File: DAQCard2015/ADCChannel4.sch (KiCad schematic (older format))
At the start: 50 parts, among them U1 LTC6403, U2 AD9219, U3 LTC6403, U4 LTC6403, U5 LTC6403

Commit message: Updates to DAQ Card including FPGA card pinout and completion of ADC Stage
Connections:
- net labels added: 18ana

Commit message: Replaces single ample with 4-channel varients. Greatly reducing part count
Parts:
- removed C1, C11, C15, C16: .01uF, symbol C
- removed C10, C2, C3, C7, C9: .1uF, symbol C
- removed C12, C13, C14, C17, C18, C19, C20, C21, C4, C5, C6: C, symbol C
- removed C8: 2.2uF, symbol CP
- removed R1, R13, R14, R8: Rt, symbol R
- removed R10, R15, R16, R17, R2, R3, R9: Ri, symbol R
- removed R11, R12, R5, R6: Rf, symbol R
- removed R7: 10k, symbol R
- removed U1, U3, U4, U5: LTC6403, symbol LTC6403
- removed U2: AD9219, symbol AD9219
- added C23, C24: C, symbol C
- added C25: .01uF, symbol C
- added C26, C27, C28, C30, C31: .1uF, symbol C
- added C29: 2.2uF, symbol CP
- added RP7: R_PACK8, symbol R_PACK8
- added RP8, RP9: Rf, symbol R_PACK4
- added U6: THS4524IDBTR, symbol THS4524IDBTR
- added U7: AD9219, symbol AD9219
- R18: value Ri -> Rt
- R19, R20, R21: value Rf -> Rt
- R22: value Rf -> 2.7k
- R23: value 2.7k -> 1k
- R24: value 1k -> 10k
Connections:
- net labels added: 3V3ana, VOCM
- net labels removed: 18ana, 3V3, Vocm
- wire segments 178 -> 192
- no-connect marks 12 -> 4

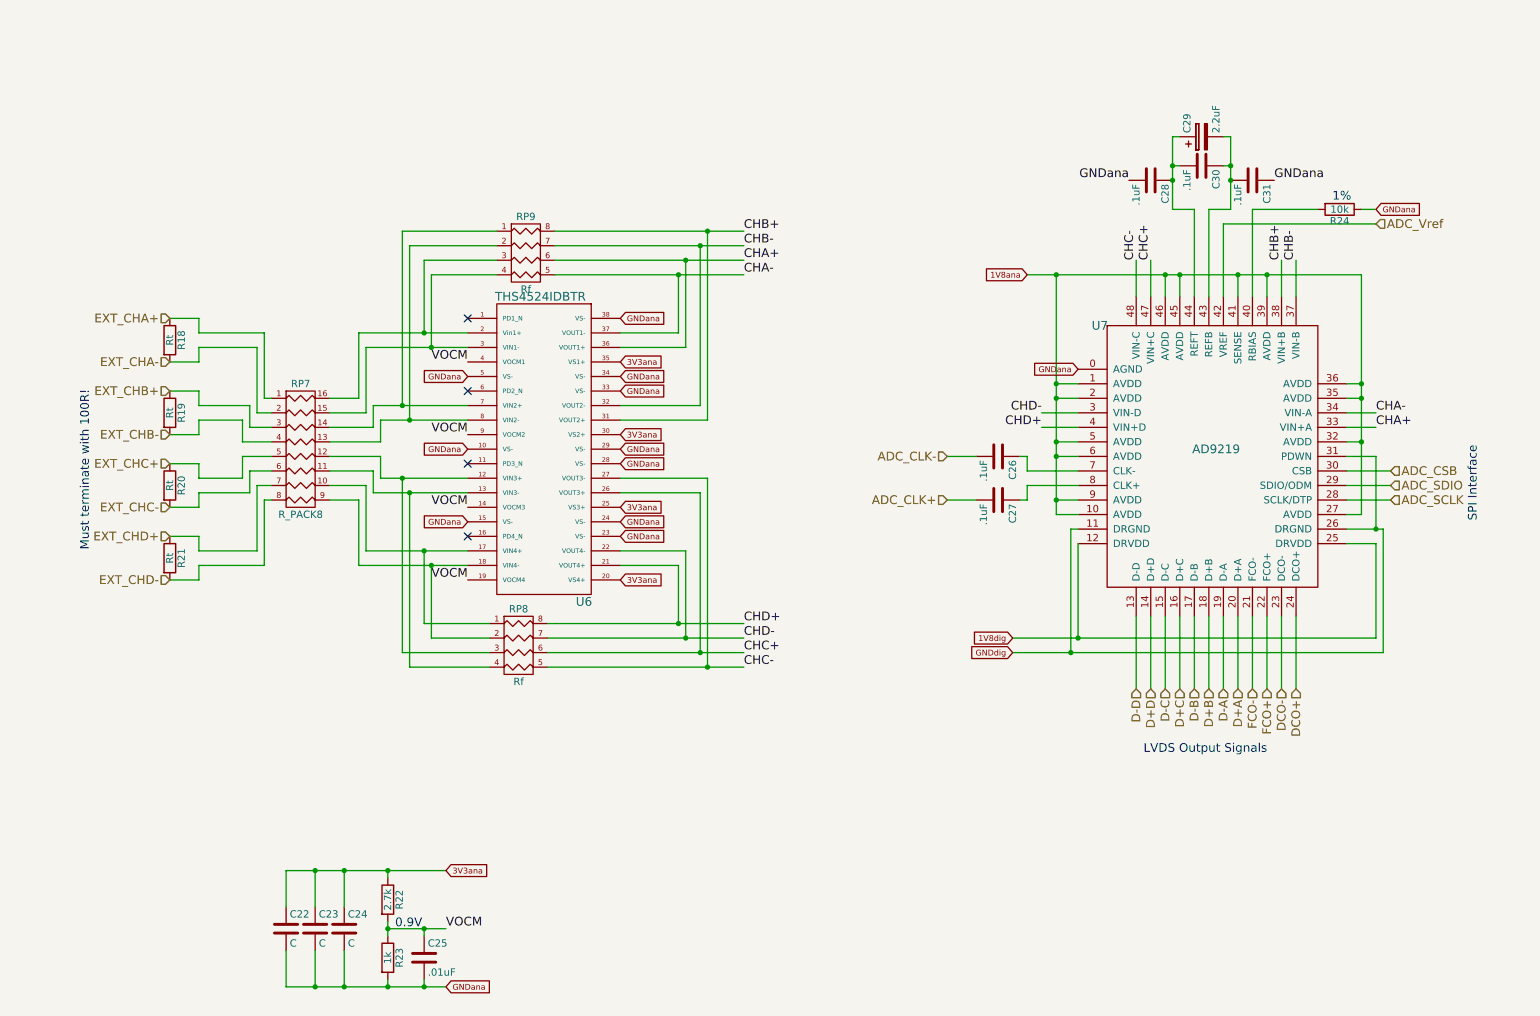
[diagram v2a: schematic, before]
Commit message: Finishes initial version of schematic(mostly). And adds a whole bunch of new footprints!
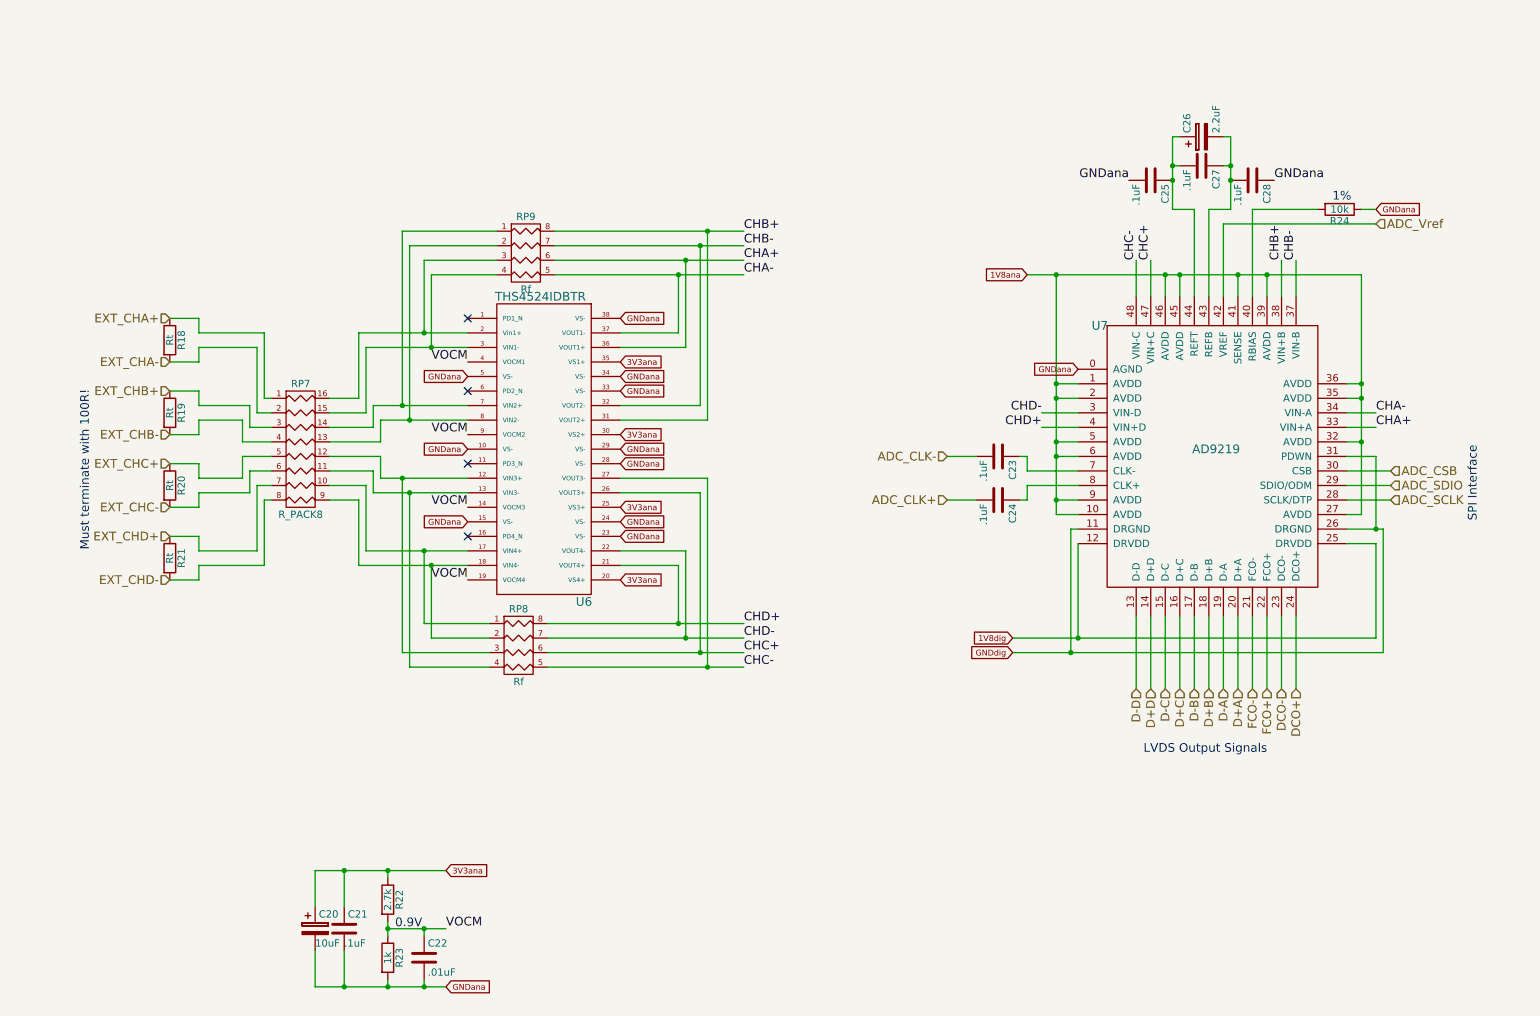
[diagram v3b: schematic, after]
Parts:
- removed C26, C30, C31: .1uF, symbol C
- removed C29: 2.2uF, symbol CP
- added C20: 10uF, extras:SMD_Cap_3mmDia, symbol CP
- added C21: .1uF, Capacitors_SMD:C_0603, symbol C
- added C26: 2.2uF, extras:SMD_Cap_3mmDia, symbol CP
- C22: value C -> .01uF; footprint (none) -> Capacitors_SMD:C_0603
- C23, C24: value C -> .1uF; footprint (none) -> Capacitors_SMD:C_0603
- C25: value .01uF -> .1uF; footprint (none) -> Capacitors_SMD:C_0603
- C27, C28: footprint (none) -> Capacitors_SMD:C_0603
- R18, R19, R20, R21, R22, R23, R24: footprint (none) -> Resistors_SMD:R_0603
- RP7: footprint (none) -> extras:R8_MNR18
- RP8, RP9: footprint (none) -> extras:R4-MNR04
- U6: footprint (none) -> Housings_SSOP:TSSOP-38_4.4x9.7mm_Pitch0.5mm
- U7: footprint (none) -> SMD_Packages:QFN-48-1EP
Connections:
- net 3V3ana: now also C20.1, C21.1; no longer C22.1, C23.1, C24.1
- net ADC_CLK+: now also C24.2; no longer C27.2
- net ADC_CLK-: now also C23.2
- net GNDana: now also C28.1, C20.2, C21.2; no longer C23.2, C24.2, C28.2
- net VOCM: now also C22.1; no longer C25.1
- net at U7.43 (REFB): now also C27.1, C28.2, C26.2
- net at U7.44 (REFT): now also C25.1, C27.2, C26.1; no longer C28.1
- net at U7.7 (CLK-): now also C23.1
- net at U7.8 (CLK+): now also C24.1; no longer C27.1
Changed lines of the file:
@@
 $Comp
 L AD9219 U7
-U 1 1 55CFF5AC
+U 1 1 55CB5755
 P 9050 3700
 F 0 "U7" H 8250 4650 60  0000 C CNN
 F 1 "AD9219" H 9050 3800 60  0000 C CNN
-F 2 "" H 8650 3700 60  0000 C CNN
+F 2 "SMD_Packages:QFN-48-1EP" H 8650 3700 60  0001 C CNN
 F 3 "" H 8650 3700 60  0000 C CNN
 	1    9050 3700
@@
 $Comp
 L R R22
-U 1 1 55CE40F6
+U 1 1 55CFF5F5
 P 3350 6700
 F 0 "R22" V 3430 6700 50  0000 C CNN
 F 1 "2.7k" V 3350 6700 50  0000 C CNN
-F 2 "" V 3280 6700 30  0000 C CNN
+F 2 "Resistors_SMD:R_0603" V 3280 6700 30  0001 C CNN
 F 3 "" H 3350 6700 30  0000 C CNN
 	1    3350 6700
@@
 $Comp
 L R R23
-U 1 1 55CFF5DD
+U 1 1 55CB577B
 P 3350 7100
 F 0 "R23" V 3430 7100 50  0000 C CNN
 F 1 "1k" V 3350 7100 50  0000 C CNN
-F 2 "" V 3280 7100 30  0000 C CNN
+F 2 "Resistors_SMD:R_0603" V 3280 7100 30  0001 C CNN
 F 3 "" H 3350 7100 30  0000 C CNN
 	1    3350 7100
@@
 Must terminate with 100R!
 $Comp
-L C C22
-U 1 1 55CFF5C7
-P 2650 6900
-F 0 "C22" H 2675 7000 50  0000 L CNN
-F 1 "C" H 2675 6800 50  0000 L CNN
-F 2 "" H 2688 6750 30  0000 C CNN
-F 3 "" H 2650 6900 60  0000 C CNN
-	1    2650 6900
-	1    0    0    -1
-$EndComp
-$Comp
-L C C23
-U 1 1 55CFF5B6
-P 2850 6900
-F 0 "C23" H 2875 7000 50  0000 L CNN
-F 1 "C" H 2875 6800 50  0000 L CNN
-F 2 "" H 2888 6750 30  0000 C CNN
-F 3 "" H 2850 6900 60  0000 C CNN
-	1    2850 6900
-	1    0    0    -1
-$EndComp
-$Comp
-L C C24
-U 1 1 55CFF5BD
+L C C21
+U 1 1 55CB5760
 P 3050 6900
-F 0 "C24" H 3075 7000 50  0000 L CNN
-F 1 "C" H 3075 6800 50  0000 L CNN
-F 2 "" H 3088 6750 30  0000 C CNN
+F 0 "C21" H 3075 7000 50  0000 L CNN
+F 1 ".1uF" H 3050 6800 50  0000 L CNN
+F 2 "Capacitors_SMD:C_0603" H 3088 6750 30  0001 C CNN
 F 3 "" H 3050 6900 60  0000 C CNN
 	1    3050 6900
@@
 ADC_SCLK
 $Comp
-L C C26
-U 1 1 55CFF5C0
+L C C23
+U 1 1 55CFF5C6
 P 7550 3650
-F 0 "C26" H 7575 3750 50  0000 L CNN
+F 0 "C23" H 7575 3750 50  0000 L CNN
 F 1 ".1uF" H 7575 3550 50  0000 L CNN
-F 2 "" H 7588 3500 30  0000 C CNN
+F 2 "Capacitors_SMD:C_0603" H 7588 3500 30  0001 C CNN
 F 3 "" H 7550 3650 60  0000 C CNN
 	1    7550 3650
@@
 $EndComp
 $Comp
-L C C27
-U 1 1 55CFF5E8
+L C C24
+U 1 1 55CB574A
 P 7550 3950
-F 0 "C27" H 7575 4050 50  0000 L CNN
+F 0 "C24" H 7575 4050 50  0000 L CNN
 F 1 ".1uF" H 7575 3850 50  0000 L CNN
-F 2 "" H 7588 3800 30  0000 C CNN
+F 2 "Capacitors_SMD:C_0603" H 7588 3800 30  0001 C CNN
 F 3 "" H 7550 3950 60  0000 C CNN
 	1    7550 3950
@@
 DCO+
 $Comp
-L C C31
-U 1 1 55CFF5F9
+L C C28
+U 1 1 55CB578D
 P 9300 1750
-F 0 "C31" H 9325 1850 50  0000 L CNN
+F 0 "C28" H 9325 1850 50  0000 L CNN
 F 1 ".1uF" H 9325 1650 50  0000 L CNN
-F 2 "" H 9338 1600 30  0000 C CNN
+F 2 "Capacitors_SMD:C_0603" H 9338 1600 30  0001 C CNN
 F 3 "" H 9300 1750 60  0000 C CNN
 	1    9300 1750
@@
 $EndComp
 $Comp
-L C C28
-U 1 1 55CFF5D0
+L C C25
+U 1 1 55CFF5CE
 P 8600 1750
-F 0 "C28" H 8625 1850 50  0000 L CNN
+F 0 "C25" H 8625 1850 50  0000 L CNN
 F 1 ".1uF" H 8625 1650 50  0000 L CNN
-F 2 "" H 8638 1600 30  0000 C CNN
+F 2 "Capacitors_SMD:C_0603" H 8638 1600 30  0001 C CNN
 F 3 "" H 8600 1750 60  0000 C CNN
 	1    8600 1750
@@
 $EndComp
 $Comp
-L C C30
-U 1 1 55CFF5D6
+L C C27
+U 1 1 55CB5775
 P 8950 1650
-F 0 "C30" H 8975 1750 50  0000 L CNN
+F 0 "C27" H 8975 1750 50  0000 L CNN
 F 1 ".1uF" H 8975 1550 50  0000 L CNN
-F 2 "" H 8988 1500 30  0000 C CNN
+F 2 "Capacitors_SMD:C_0603" H 8988 1500 30  0001 C CNN
 F 3 "" H 8950 1650 60  0000 C CNN
 	1    8950 1650
@@
 GNDana
 $Comp
-L CP C29
-U 1 1 55CFF604
+L CP C26
+U 1 1 55CB5796
 P 8950 1450
-F 0 "C29" H 8975 1550 50  0000 L CNN
+F 0 "C26" H 8975 1550 50  0000 L CNN
 F 1 "2.2uF" H 8975 1350 50  0000 L CNN
-F 2 "" H 8988 1300 30  0000 C CNN
+F 2 "extras:SMD_Cap_3mmDia" H 8988 1300 30  0001 C CNN
 F 3 "" H 8950 1450 60  0000 C CNN
 	1    8950 1450
@@
 $Comp
 L R R24
-U 1 1 55CFF5F0
+U 1 1 55CB5782
 P 9900 1950
 F 0 "R24" V 9980 1950 50  0000 C CNN
 F 1 "10k" V 9900 1950 50  0000 C CNN
-F 2 "" V 9830 1950 30  0000 C CNN
+F 2 "Resistors_SMD:R_0603" V 9830 1950 30  0001 C CNN
 F 3 "" H 9900 1950 30  0000 C CNN
 	1    9900 1950
@@
 $Comp
 L THS4524IDBTR U6
-U 1 1 55CFF60C
+U 1 1 55CFF606
 P 4400 3700
 F 0 "U6" H 4700 2750 60  0000 C CNN
 F 1 "THS4524IDBTR" H 4400 4850 60  0000 C CNN
-F 2 "" H 4600 3800 60  0000 C CNN
+F 2 "Housings_SSOP:TSSOP-38_4.4x9.7mm_Pitch0.5mm" H 4600 3800 60  0001 C CNN
 F 3 "" H 4600 3800 60  0000 C CNN
 	1    4400 3700
@@
 $EndComp
 $Comp
-L C C25
-U 1 1 55CFF60D
+L C C22
+U 1 1 55CFF610
 P 3600 7100
-F 0 "C25" H 3625 7200 50  0000 L CNN
+F 0 "C22" H 3625 7200 50  0000 L CNN
 F 1 ".01uF" H 3625 7000 50  0000 L CNN
-F 2 "" H 3638 6950 30  0000 C CNN
+F 2 "Capacitors_SMD:C_0603" H 3638 6950 30  0001 C CNN
 F 3 "" H 3600 7100 60  0000 C CNN
 	1    3600 7100
@@
 Connection ~ 3600 6900
 Wire Wire Line
-	2650 6500 3750 6500
-Wire Wire Line
 	3050 6500 3050 6750
 Connection ~ 3350 6500
@@
 Connection ~ 3050 6500
 Wire Wire Line
-	2650 6500 2650 6750
-Connection ~ 2850 6500
-Wire Wire Line
-	2650 7300 3750 7300
-Wire Wire Line
 	3050 7300 3050 7050
 Wire Wire Line
 	2850 7300 2850 7050
 Connection ~ 3050 7300
-Wire Wire Line
-	2650 7300 2650 7050
-Connection ~ 2850 7300
 Wire Wire Line
 	3600 7300 3600 7250
@@
 $Comp
 L R R21
-U 1 1 55CFF618
+U 1 1 55CB57AC
 P 1850 4350
 F 0 "R21" V 1930 4350 50  0000 C CNN
 F 1 "Rt" V 1850 4350 50  0000 C CNN
-F 2 "" V 1780 4350 30  0000 C CNN
+F 2 "Resistors_SMD:R_0603" V 1780 4350 30  0001 C CNN
 F 3 "" H 1850 4350 30  0000 C CNN
 	1    1850 4350
@@
 $Comp
 L R R20
-U 1 1 55CFF61D
+U 1 1 55CB57B4
 P 1850 3850
 F 0 "R20" V 1930 3850 50  0000 C CNN
 F 1 "Rt" V 1850 3850 50  0000 C CNN
-F 2 "" V 1780 3850 30  0000 C CNN
+F 2 "Resistors_SMD:R_0603" V 1780 3850 30  0001 C CNN
 F 3 "" H 1850 3850 30  0000 C CNN
 	1    1850 3850
@@
 $Comp
 L R R19
-U 1 1 55CFF623
+U 1 1 55CB57BB
 P 1850 3350
 F 0 "R19" V 1930 3350 50  0000 C CNN
 F 1 "Rt" V 1850 3350 50  0000 C CNN
-F 2 "" V 1780 3350 30  0000 C CNN
+F 2 "Resistors_SMD:R_0603" V 1780 3350 30  0001 C CNN
 F 3 "" H 1850 3350 30  0000 C CNN
 	1    1850 3350
@@
 $Comp
 L R R18
-U 1 1 55CF3DDC
+U 1 1 55CFF62E
 P 1850 2850
 F 0 "R18" V 1930 2850 50  0000 C CNN
 F 1 "Rt" V 1850 2850 50  0000 C CNN
-F 2 "" V 1780 2850 30  0000 C CNN
+F 2 "Resistors_SMD:R_0603" V 1780 2850 30  0001 C CNN
 F 3 "" H 1850 2850 30  0000 C CNN
 	1    1850 2850
@@
 $Comp
 L R_PACK4 RP8
-U 1 1 55CF4768
+U 1 1 55CB57C5
 P 4250 5150
 F 0 "RP8" H 4250 5600 50  0000 C CNN
 F 1 "Rf" H 4250 5100 50  0000 C CNN
-F 2 "" H 4250 5150 60  0000 C CNN
+F 2 "extras:R4-MNR04" H 4250 5150 60  0001 C CNN
 F 3 "" H 4250 5150 60  0000 C CNN
 	1    4250 5150
@@
 $Comp
 L R_PACK4 RP9
-U 1 1 55CFF637
+U 1 1 55CB574E
 P 4300 2450
 F 0 "RP9" H 4300 2900 50  0000 C CNN
 F 1 "Rf" H 4300 2400 50  0000 C CNN
-F 2 "" H 4300 2450 60  0000 C CNN
+F 2 "extras:R4-MNR04" H 4300 2450 60  0001 C CNN
 F 3 "" H 4300 2450 60  0000 C CNN
 	1    4300 2450
@@
 $Comp
 L R_PACK8 RP7
-U 1 1 55CFF644
+U 1 1 55CB57CC
 P 2750 3600
 F 0 "RP7" H 2750 4050 50  0000 C CNN
 F 1 "R_PACK8" H 2750 3150 50  0000 C CNN
-F 2 "" H 2750 3600 60  0000 C CNN
+F 2 "extras:R8_MNR18" H 2750 3600 60  0001 C CNN
 F 3 "" H 2750 3600 60  0000 C CNN
 	1    2750 3600
@@
 Text GLabel 10150 1950 2    40   Input ~ 0
 GNDana
+Wire Wire Line
+	3750 6500 2850 6500
+Wire Wire Line
+	2850 7300 3750 7300
+$Comp
+L CP C20
+U 1 1 55CB573E
+P 2850 6900
+F 0 "C20" H 2875 7000 50  0000 L CNN
+F 1 "10uF" H 2850 6800 50  0000 L CNN
+F 2 "extras:SMD_Cap_3mmDia" H 2888 6750 30  0001 C CNN
+F 3 "" H 2850 6900 60  0000 C CNN
+	1    2850 6900
+	1    0    0    -1
+$EndComp
 $EndSCHEMATC

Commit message: Adds a more-or-less complete BOM to DAQ Card
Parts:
- C22: value .01uF -> 10000pF
- RP7: value R_PACK8 -> Ri
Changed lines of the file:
@@
 $Descr A4 11693 8268
 encoding utf-8
-Sheet 3 13
+Sheet 5 13
 Title ""
 Date ""
@@
 P 3600 7100
 F 0 "C22" H 3625 7200 50  0000 L CNN
-F 1 ".01uF" H 3625 7000 50  0000 L CNN
+F 1 "10000pF" H 3625 7000 50  0000 L CNN
 F 2 "Capacitors_SMD:C_0603" H 3638 6950 30  0001 C CNN
 F 3 "" H 3600 7100 60  0000 C CNN
@@
 P 2750 3600
 F 0 "RP7" H 2750 4050 50  0000 C CNN
-F 1 "R_PACK8" H 2750 3150 50  0000 C CNN
+F 1 "Ri" H 2750 3150 50  0000 C CNN
 F 2 "extras:R8_MNR18" H 2750 3600 60  0001 C CNN
 F 3 "" H 2750 3600 60  0000 C CNN

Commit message: Updates to DAQCard2015, especially to power systems
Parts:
- C20, C26: footprint extras:SMD_Cap_3mmDia -> Capacitors_SMD:C_0805
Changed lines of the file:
@@
 F 0 "C26" H 8975 1550 50  0000 L CNN
 F 1 "2.2uF" H 8975 1350 50  0000 L CNN
-F 2 "extras:SMD_Cap_3mmDia" H 8988 1300 30  0001 C CNN
+F 2 "Capacitors_SMD:C_0805" H 8988 1300 30  0001 C CNN
 F 3 "" H 8950 1450 60  0000 C CNN
 	1    8950 1450
@@
 F 0 "C20" H 2875 7000 50  0000 L CNN
 F 1 "10uF" H 2850 6800 50  0000 L CNN
-F 2 "extras:SMD_Cap_3mmDia" H 2888 6750 30  0001 C CNN
+F 2 "Capacitors_SMD:C_0805" H 2888 6750 30  0001 C CNN
 F 3 "" H 2850 6900 60  0000 C CNN
 	1    2850 6900
